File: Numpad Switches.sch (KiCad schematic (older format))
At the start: 84 parts

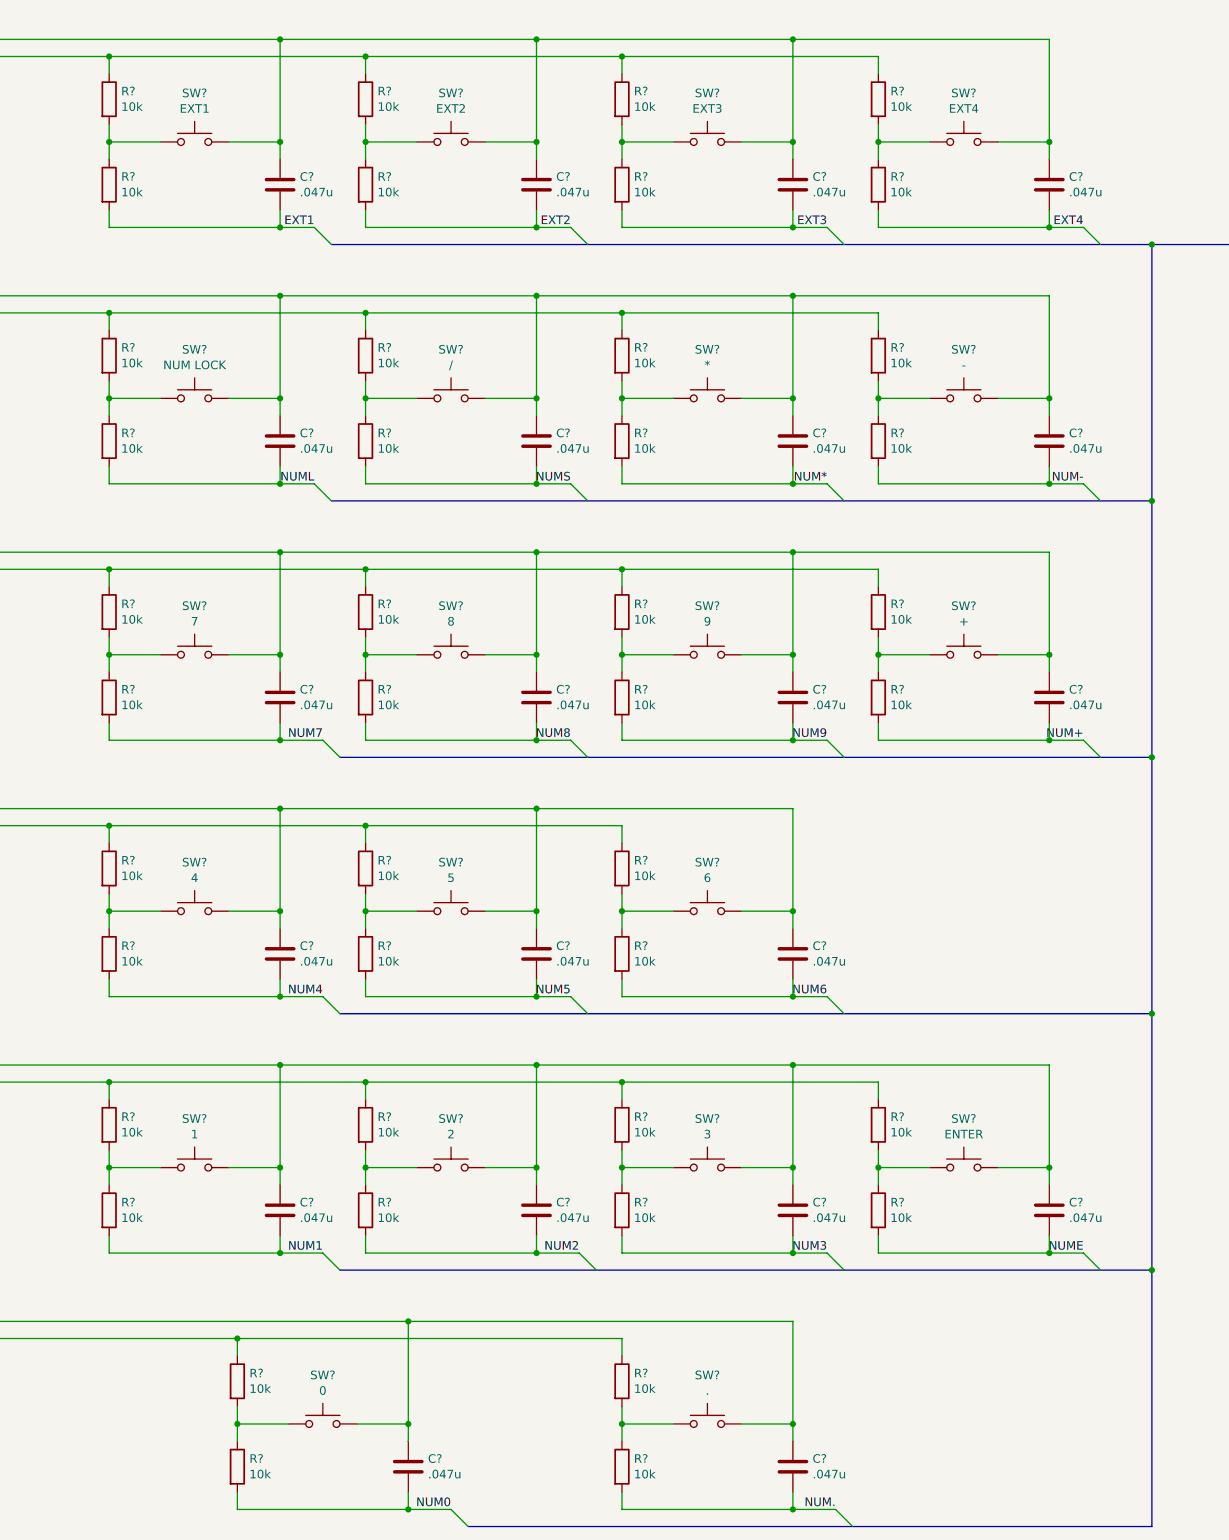
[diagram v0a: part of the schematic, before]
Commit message: Corrected errors found in design rule check
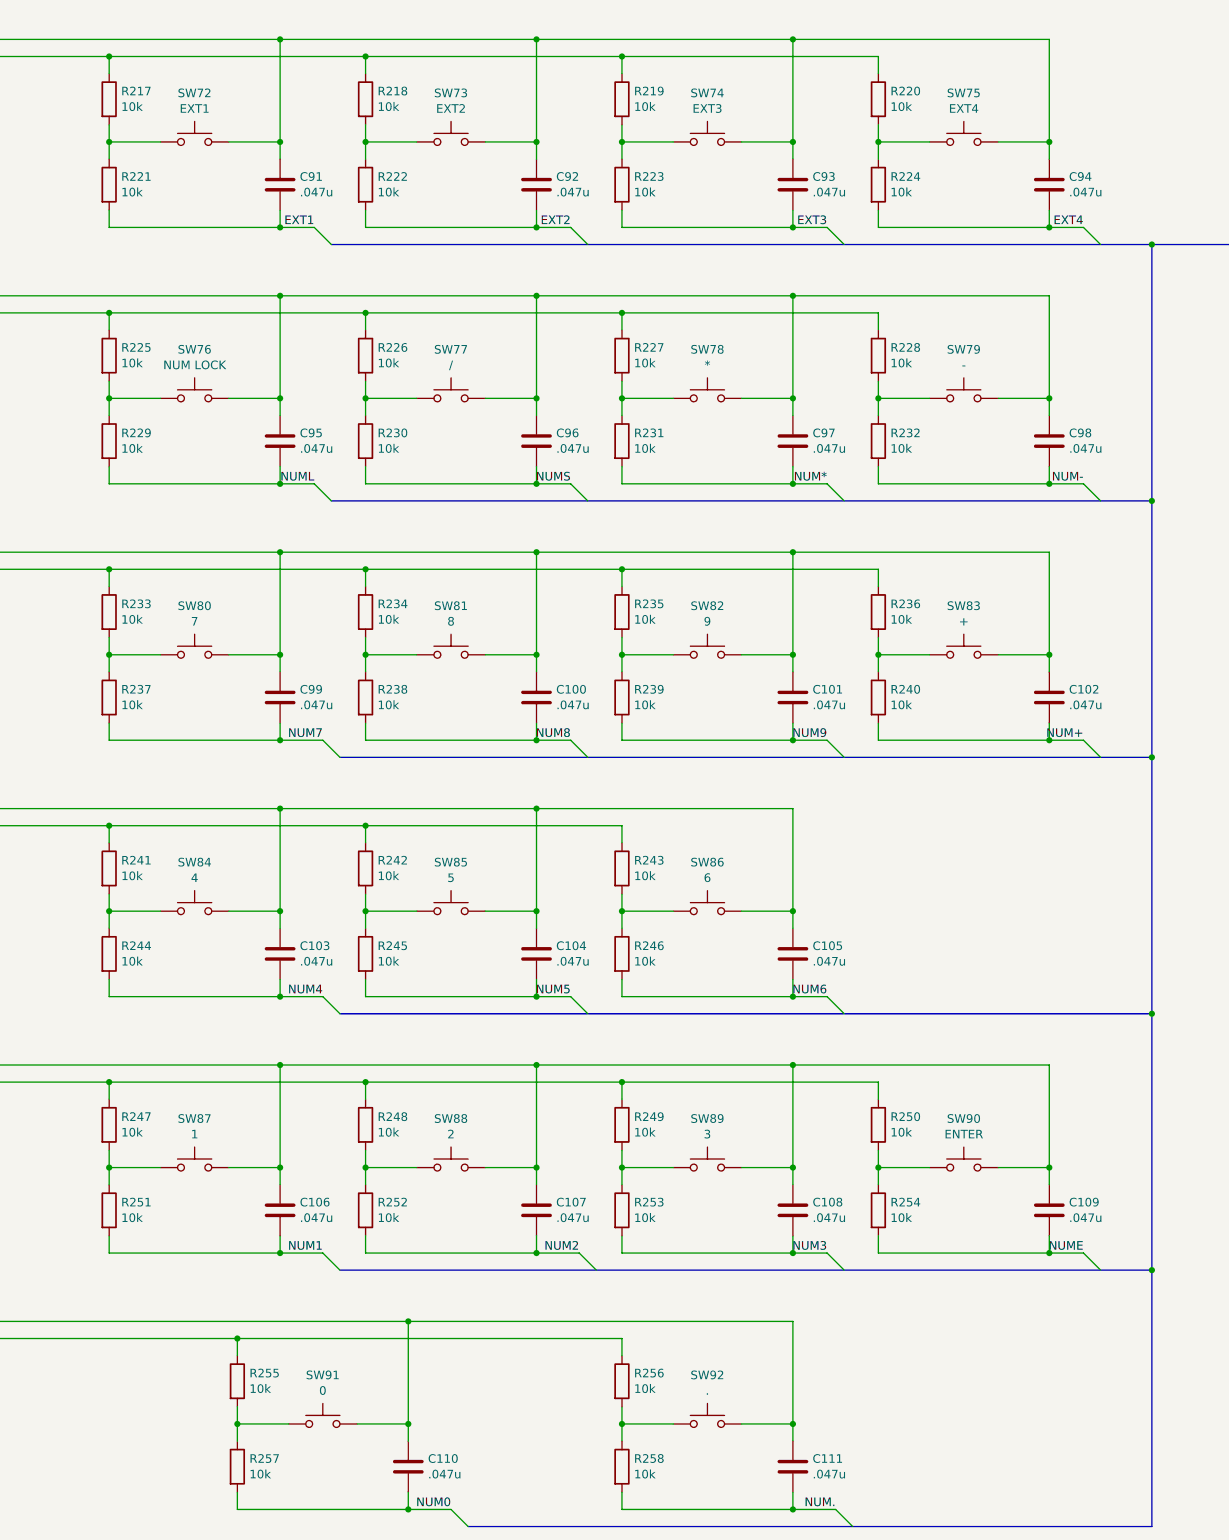
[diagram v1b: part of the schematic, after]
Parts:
- C100, C101, C102, C103, C104, C105, C106, C107, C108, C109, C110, C111, C91, C92, C93, C94, C95, C96, C97, C98, C99: renamed from C?; footprint (none) -> Capacitor_SMD:C_1206_3216Metric_Pad1.42x1.75mm_HandSolder
- R217, R218, R219, R220, R221, R222, R223, R224, R225, R226, R227, R228, R229, R230, R231, R232, R233, R234, R235, R236, R237, R238, R239, R240, R241, R242, R243, R244, R245, R246, R247, R248, R249, R250, R251, R252, R253, R254, R255, R256, R257, R258: renamed from R?; footprint (none) -> Resistor_SMD:R_1206_3216Metric_Pad1.42x1.75mm_HandSolder
- SW72, SW73, SW74, SW75, SW76, SW77, SW78, SW79, SW80, SW81, SW82, SW83, SW84, SW85, SW86, SW87, SW88, SW89, SW90, SW91, SW92: renamed from SW?; footprint (none) -> Button_Switch_Keyboard:SW_Cherry_MX_1.00u_PCB

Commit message: Redesigned for single large PCB
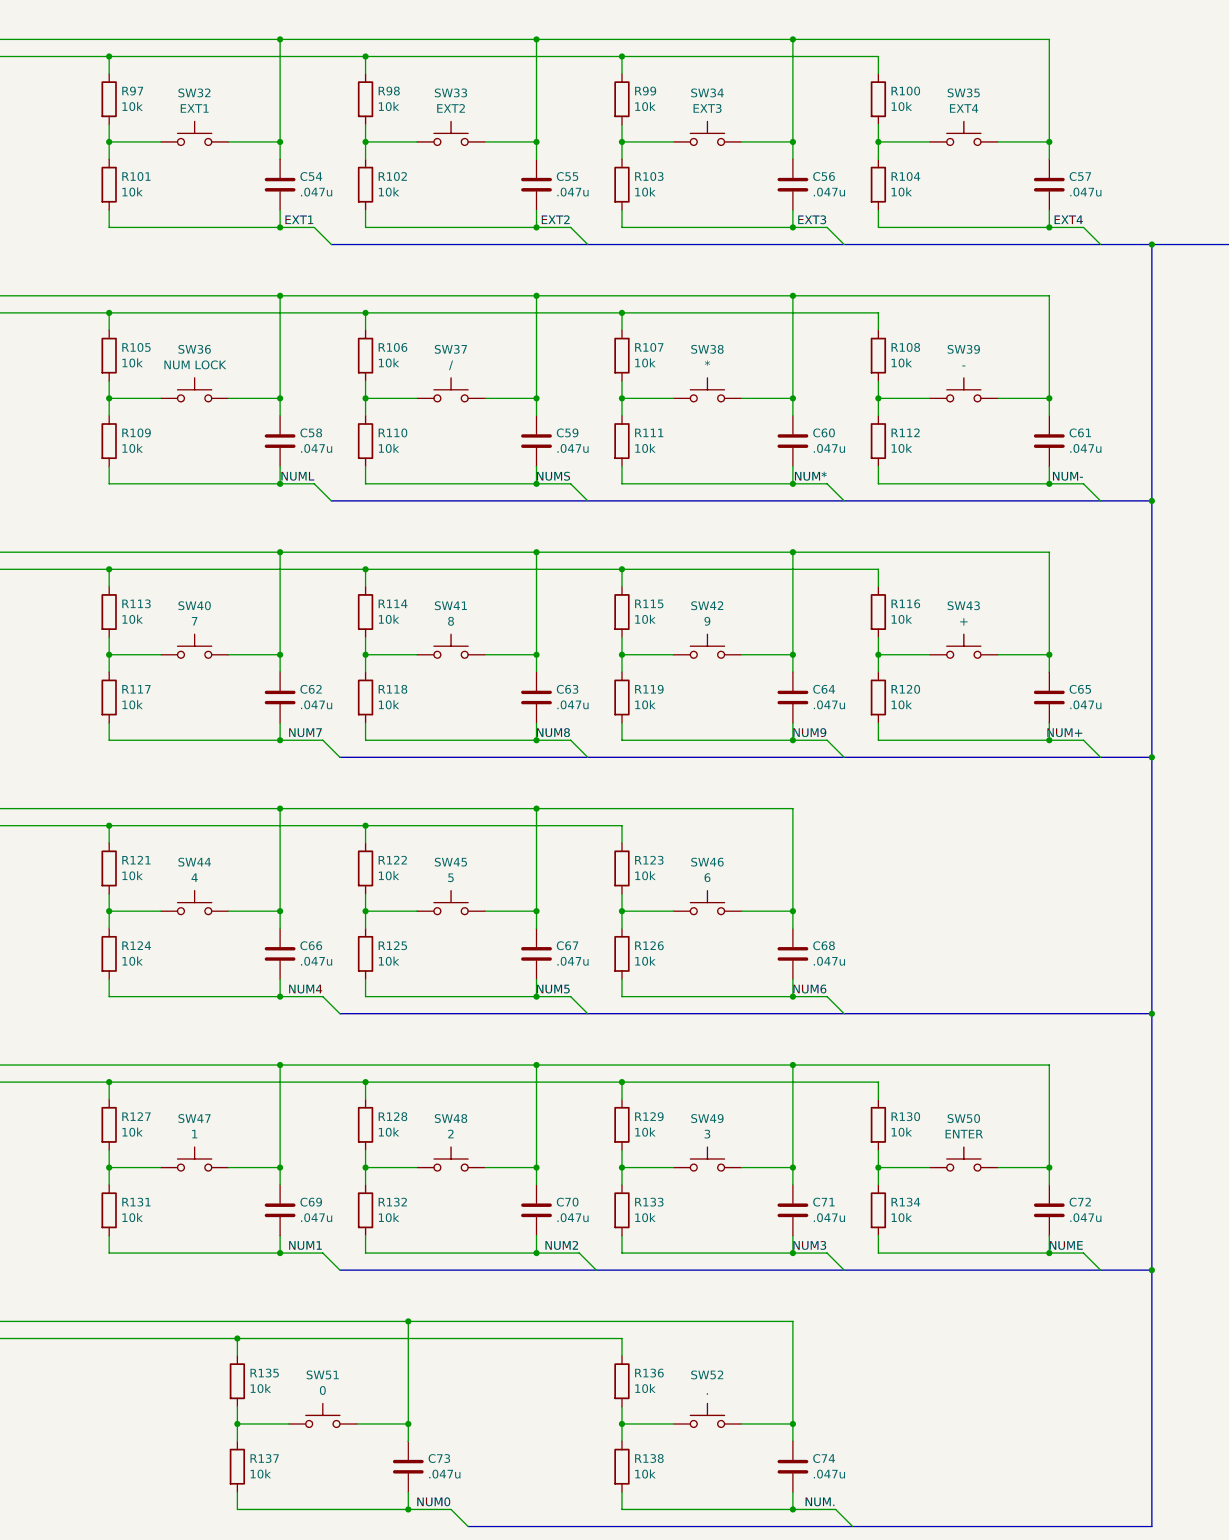
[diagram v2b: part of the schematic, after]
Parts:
- renumbered C91 to C54, C92 to C55, C93 to C56, C94 to C57, C95 to C58, C96 to C59, C97 to C60, C98 to C61, C99 to C62, C100 to C63, C101 to C64, C102 to C65, C103 to C66, C104 to C67, C105 to C68, C106 to C69, C107 to C70, C108 to C71, C109 to C72, C110 to C73, C111 to C74, R220 to R100, R221 to R101, R222 to R102, R223 to R103, R224 to R104, R225 to R105, R226 to R106, R227 to R107, R228 to R108, R229 to R109, R230 to R110, R231 to R111, R232 to R112, R233 to R113, R234 to R114, R235 to R115, R236 to R116, R237 to R117, R238 to R118, R239 to R119, R240 to R120, R241 to R121, R242 to R122, R243 to R123, R244 to R124, R245 to R125, R246 to R126, R247 to R127, R248 to R128, R249 to R129, R250 to R130, R251 to R131, R252 to R132, R253 to R133, R254 to R134, R255 to R135, R256 to R136, R257 to R137, R258 to R138, R217 to R97, R218 to R98, R219 to R99, SW72 to SW32, SW73 to SW33, SW74 to SW34, SW75 to SW35, SW76 to SW36, SW77 to SW37, SW78 to SW38, SW79 to SW39, SW80 to SW40, SW81 to SW41, SW82 to SW42, SW83 to SW43, SW84 to SW44, SW85 to SW45, SW86 to SW46, SW87 to SW47, SW88 to SW48, SW89 to SW49, SW90 to SW50, SW91 to SW51, SW92 to SW52
